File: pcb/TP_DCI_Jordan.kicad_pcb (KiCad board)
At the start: 2 copper layers, 62 x 33 mm, 19 parts, among them J1 MICRO, J2 Display, SW1 SW_DIP_x03, U1 PCF8574

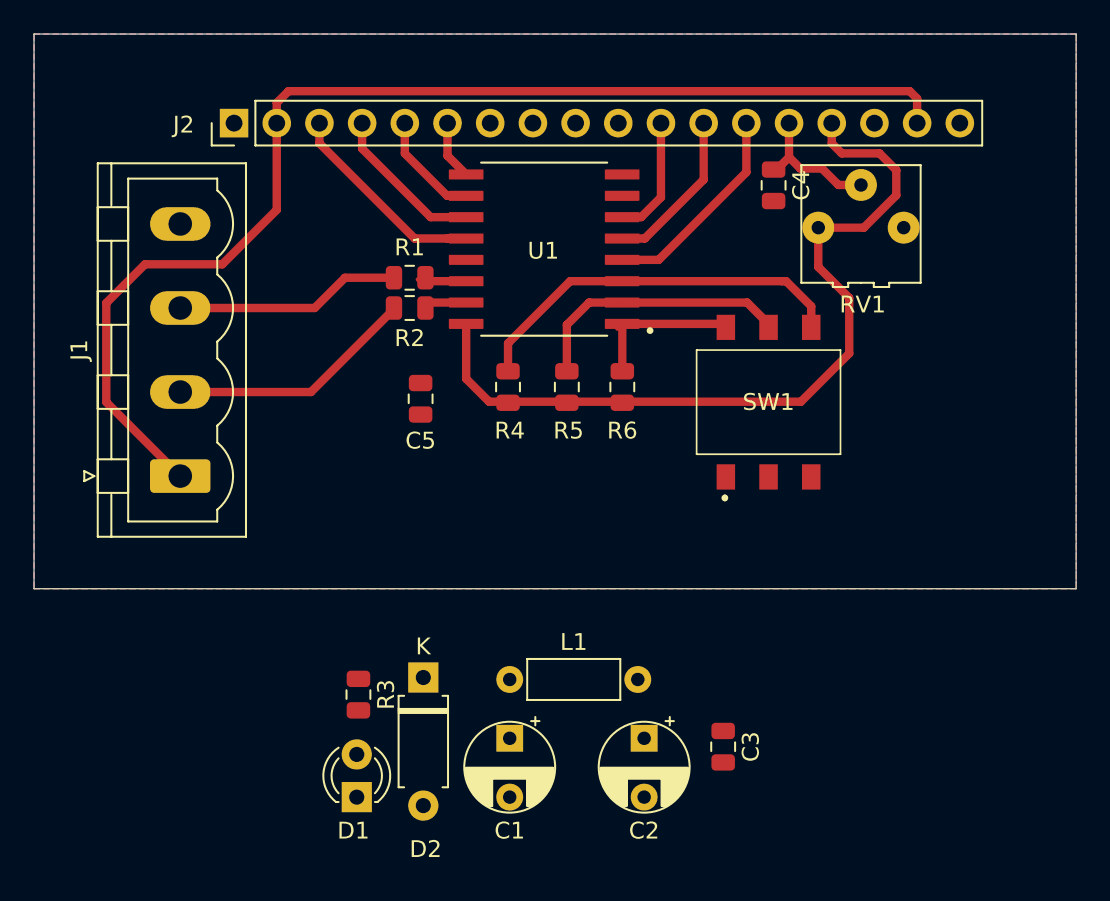
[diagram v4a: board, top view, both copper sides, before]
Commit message: actualización PCB con elementos SMD correctos
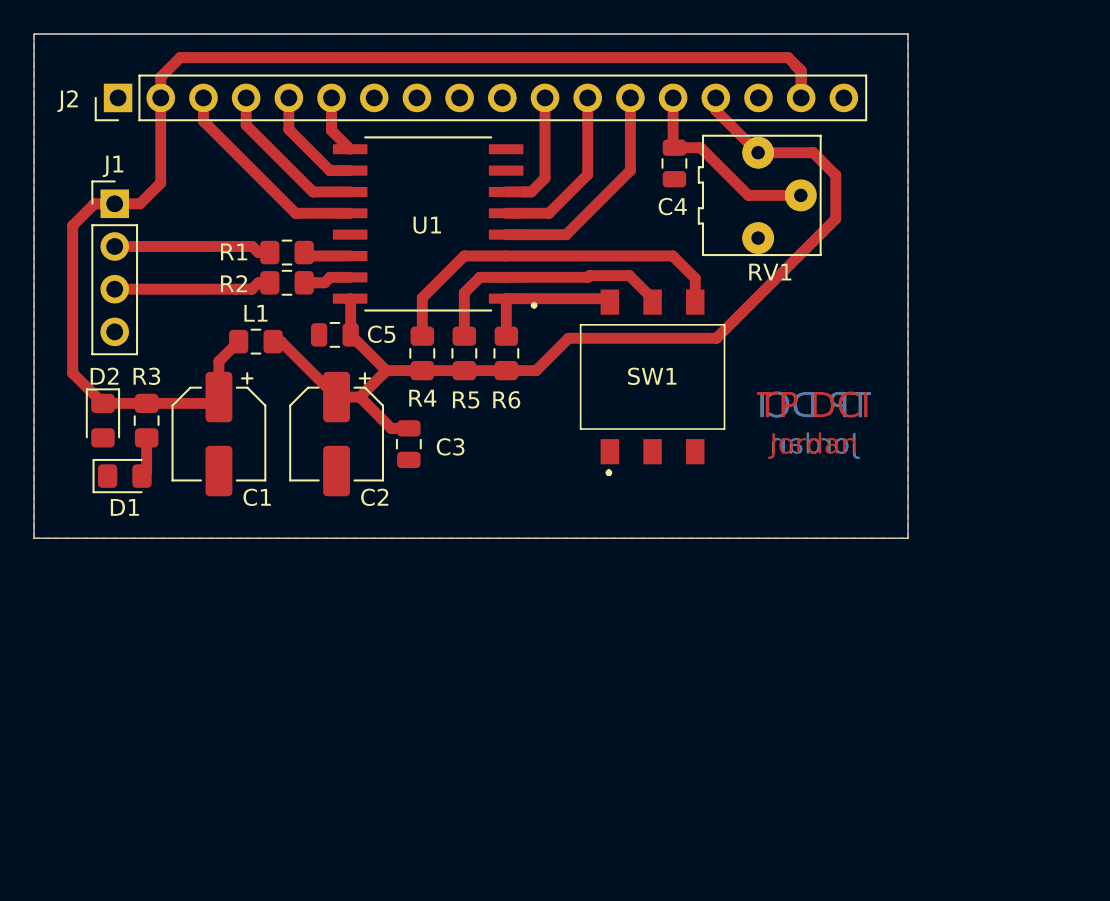
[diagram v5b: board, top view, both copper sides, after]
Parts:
- C1, C2: footprint miCapacitor_THT:Electrolitico_10uF -> Capacitor_SMD:CP_Elec_5x3.9
- D1: footprint LED_THT:LED_D3.0mm_Clear -> LED_SMD:LED_0805_2012Metric_Pad1.15x1.40mm_HandSolder
- D2: footprint miDiodo:miZener -> Diode_SMD:D_0805_2012Metric_Pad1.15x1.40mm_HandSolder
- J1: footprint Connector_Phoenix_MSTB:PhoenixContact_MSTBVA_2,5_4-G_1x04_P5.00mm_Vertical -> Connector_PinHeader_2.54mm:PinHeader_1x04_P2.54mm_Vertical
- L1: footprint Inductor_THT:L_Axial_L5.3mm_D2.2mm_P7.62mm_Horizontal_Vishay_IM-1 -> Inductor_SMD:L_0805_2012Metric_Pad1.15x1.40mm_HandSolder
- R1, R2, R3, R4, R5, R6: footprint Resistor_SMD:R_0805_2012Metric -> Resistor_SMD:R_0805_2012Metric_Pad1.15x1.40mm_HandSolder
- moved D2 27.9 mm to (191.1, 65.0)
- moved C2 26.1 mm to (205.0, 65.8)
- moved C3 26.0 mm to (209.3, 66.4)
- moved C1 25.4 mm to (198.0, 65.8)
- moved L1 25.1 mm to (200.2, 60.3)
- moved D1 23.6 mm to (192.4, 68.3), turned to 0 degrees
- moved R3 20.6 mm to (193.7, 65.0)
- moved J1 16.7 mm to (191.8, 52.1), turned to 0 degrees
- moved R1 7.45 mm to (202.1, 55.0)
- moved R2 7.45 mm to (202.1, 56.8)
- moved R6 7.18 mm to (215.1, 61.0)
- moved J2 7.06 mm to (192.0, 45.8)
- moved U1 7.06 mm to (210.4, 53.3)
- moved SW1 7.06 mm to (223.8, 62.4)
- moved R5 6.42 mm to (212.6, 61.0)
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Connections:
- J1 pad 2: /SDA -> /SCL
- J1 pad 3: /SCL -> /SDA
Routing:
- net VDD: track 48.7 -> 61.0 mm
- net /Vin: track 71.0 -> 77.5 mm
- net /SDA: track 14.8 -> 9.38 mm
- net /SCL: track 13.5 -> 9.37 mm
- net /V0: track 8.29 -> 11.7 mm
- net Net-(D1-Pad2): track 0.00 -> 2.39 mm
- net Net-(R4-Pad1): track 23.2 -> 21.5 mm
- net Net-(R5-Pad1): track 16.1 -> 15.0 mm
- net Net-(R6-Pad1): track 9.55 -> 8.50 mm
- net /RS: track 12.5 -> 13.3 mm
- net Net-(R2-Pad2): track 2.87 -> 3.58 mm
- net /R-W: track 9.66 -> 10.4 mm
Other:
- board size 62 x 33 mm -> 52 x 30 mm
- net class Default: clearance 0.4 -> 0.5; trace_width 0.5 -> 0.65
- rule trace_clearance: 0.4 -> 0.5
- board text added: "Jordan"
- board text added: "TP DCI"

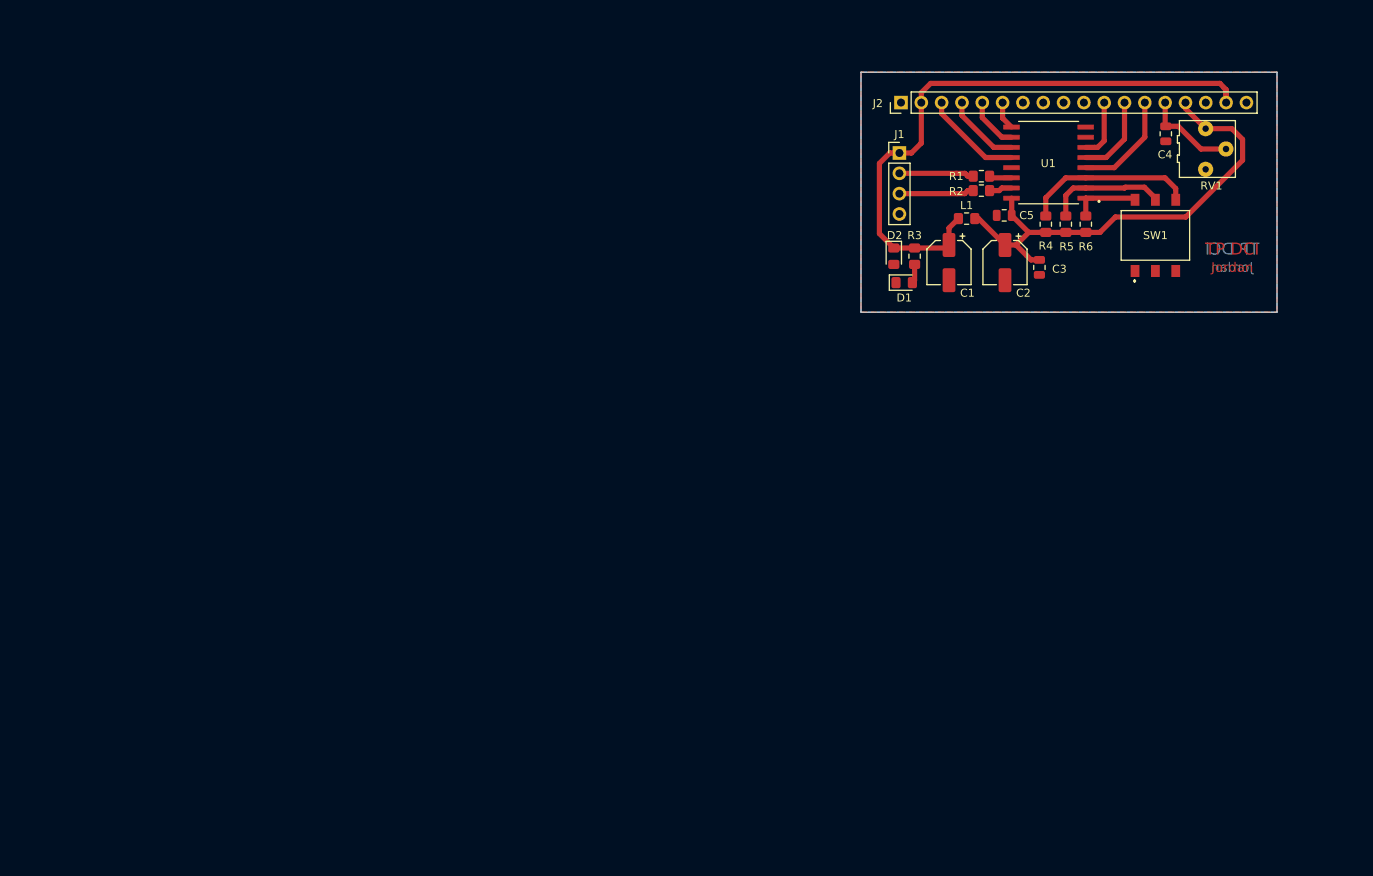
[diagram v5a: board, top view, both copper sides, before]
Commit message: se acomoda serigrafía en PCB
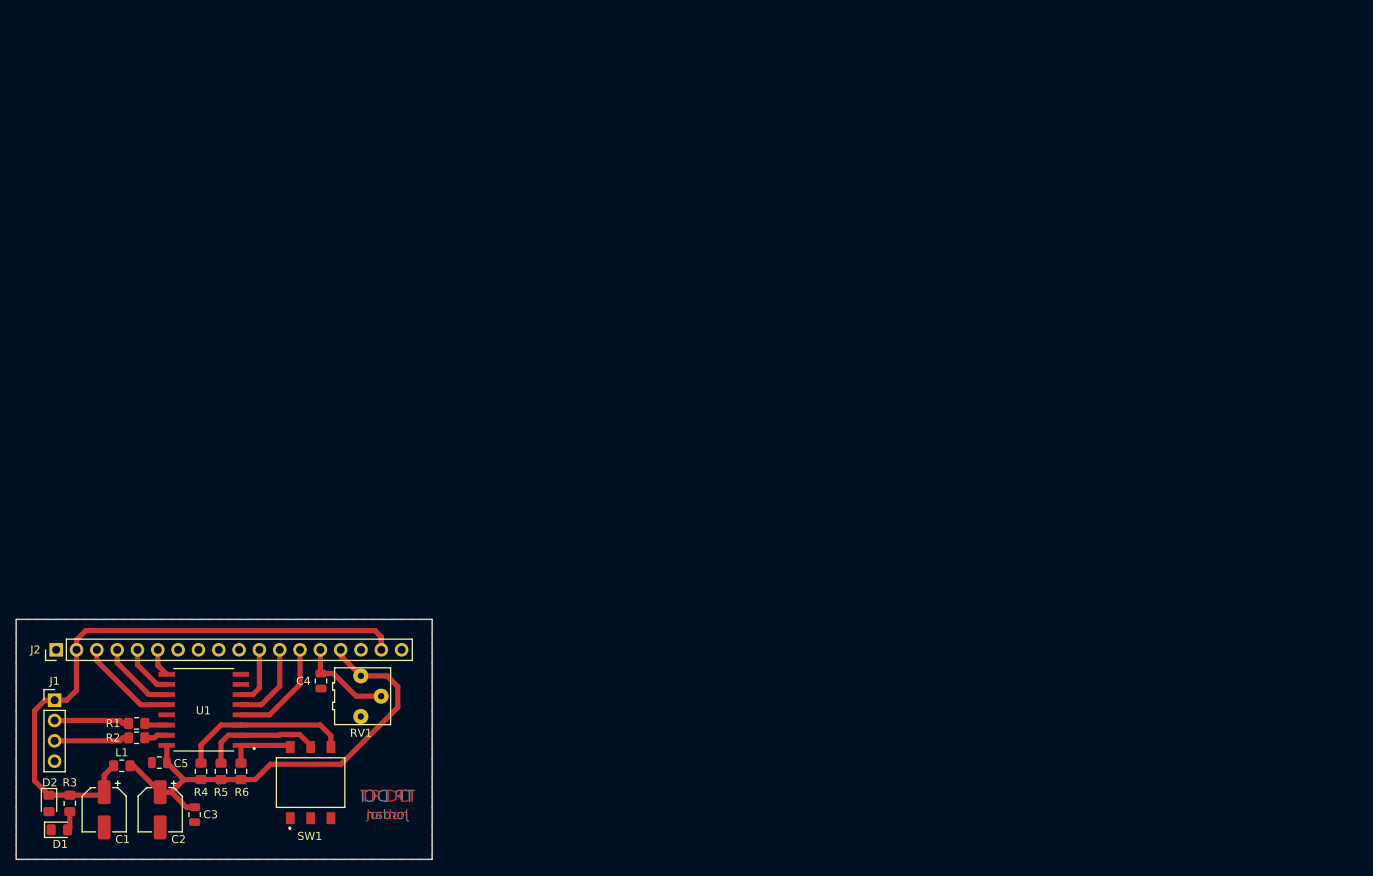
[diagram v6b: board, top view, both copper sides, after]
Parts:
- moved C3 125.8 mm to (103.7, 134.8)
- moved C5 125.8 mm to (99.3, 128.3)
- moved J1 125.8 mm to (86.2, 120.5)
- moved R1 125.8 mm to (96.5, 123.4)
- moved R2 125.8 mm to (96.5, 125.2)
- moved RV1 125.8 mm to (124.7, 120.0)
- moved SW1 125.8 mm to (118.2, 130.8)
- moved C1 125.8 mm to (92.4, 134.2)
- moved C2 125.8 mm to (99.4, 134.2)
- moved C4 125.8 mm to (119.5, 118.1)
- moved D1 125.8 mm to (86.8, 136.7)
- moved D2 125.8 mm to (85.5, 133.4)
- moved J2 125.8 mm to (86.4, 114.2)
- moved L1 125.8 mm to (94.6, 128.7)
- moved R3 125.8 mm to (88.1, 133.4)
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
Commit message: carpetas doc e info ok
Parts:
- moved R1 0.25 mm to (96.3, 123.2)
- moved R2 0.18 mm to (96.3, 125.3)
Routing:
- net /Vin: track 77.5 -> 75.4 mm
- net Net-(R4-Pad1): track 21.5 -> 23.4 mm
- net Net-(R2-Pad2): track 3.58 -> 3.06 mm
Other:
- net class Default: clearance 0.5 -> 0.6; trace_width 0.65 -> 0.6
- rule trace_clearance: 0.5 -> 0.6
- rule trace_min: 0.2 -> 0.6
